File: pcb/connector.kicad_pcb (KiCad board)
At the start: 2 copper layers, 60 x 10 mm, 7 parts

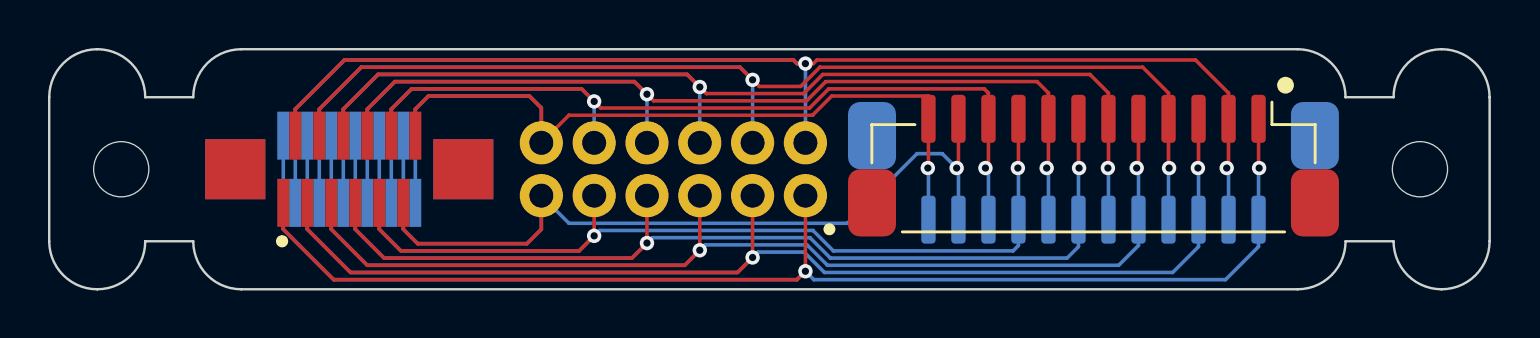
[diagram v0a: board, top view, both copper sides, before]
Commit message: small updates to silkscreen and logo
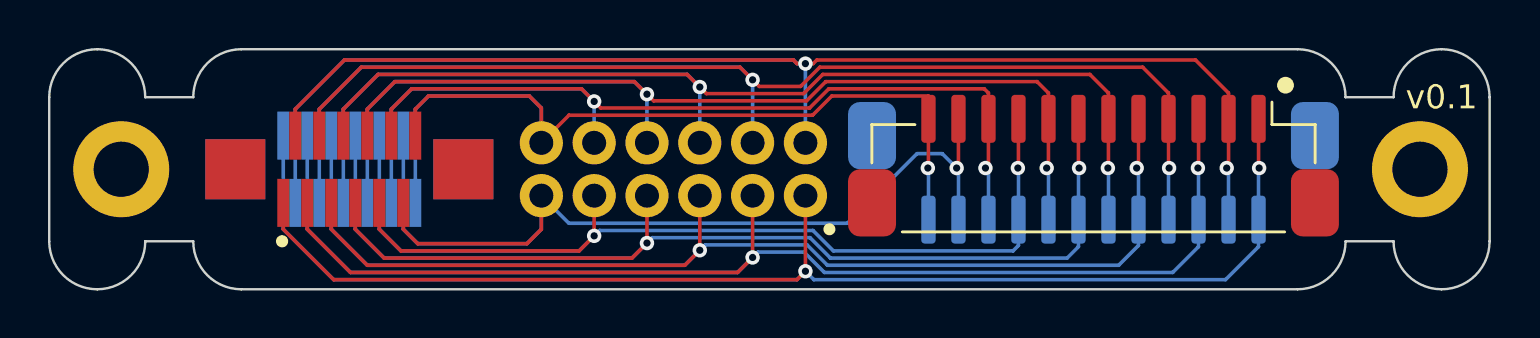
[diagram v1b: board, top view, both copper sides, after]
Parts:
- H1, H2: footprint zzkeeb:Hole_M2 -> zzkeeb:Hole_M2-TH
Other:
- board text added: "v0.1"
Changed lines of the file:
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@@
     )
   )
-  (footprint "zzkeeb:Hole_M2" (layer "F.Cu")
+  (footprint "zzkeeb:Hole_M2-TH" (layer "F.Cu")
     (at 102.583 82.516)
-    (descr "Mounting Hole 2.2mm, no annular, M2")
-    (tags "mounting hole 2.2mm no annular m2")
     (property "Sheetfile" "connector.kicad_sch")
     (property "Sheetname" "")
     (property "ki_description" "Mounting Hole without connection")
     (property "ki_keywords" "mounting hole")
-    (attr exclude_from_pos_files)
-    (fp_text reference "H1" (at -0.95 -0.55) (layer "F.Fab") hide
-        (effects (font (size 1 1) (thickness 0.15)))
-    )
-    (fp_text value "MountingHole" (at 0 0.55) (layer "F.Fab") hide
-        (effects (font (size 1 1) (thickness 0.15)))
-    )
-    (pad "" np_thru_hole circle (at 0 0) (size 2.3 2.3) (drill 2.3) (layers "*.Cu" "*.Mask"))
+    (attr through_hole)
+    (fp_text reference "H1" (at 0 2.8) (layer "F.SilkS") hide
+        (effects (font (size 1 1) (thickness 0.15)))
+    )
+    (fp_text value "MountingHole" (at 0 -2.8) (layer "F.Fab") hide
+        (effects (font (size 1 1) (thickness 0.15)))
+    )
+    (pad "" thru_hole circle (at 0 0) (size 4 4) (drill 2.3) (layers "*.Cu" "*.Mask"))
   )
   (footprint "zzkeeb:Connector_VIK-magnetic-keyboard" (layer "F.Cu")
@@
     )
   )
-  (footprint "zzkeeb:Hole_M2" (layer "F.Cu")
+  (footprint "zzkeeb:Hole_M2-TH" (layer "F.Cu")
     (at 156.683 82.516)
-    (descr "Mounting Hole 2.2mm, no annular, M2")
-    (tags "mounting hole 2.2mm no annular m2")
     (property "Sheetfile" "connector.kicad_sch")
     (property "Sheetname" "")
     (property "ki_description" "Mounting Hole without connection")
     (property "ki_keywords" "mounting hole")
-    (attr exclude_from_pos_files)
-    (fp_text reference "H2" (at -0.95 -0.55) (layer "F.Fab") hide
-        (effects (font (size 1 1) (thickness 0.15)))
-    )
-    (fp_text value "MountingHole" (at 0 0.55) (layer "F.Fab") hide
-        (effects (font (size 1 1) (thickness 0.15)))
-    )
-    (pad "" np_thru_hole circle (at 0 0) (size 2.3 2.3) (drill 2.3) (layers "*.Cu" "*.Mask"))
+    (attr through_hole)
+    (fp_text reference "H2" (at 0 2.8) (layer "F.SilkS") hide
+        (effects (font (size 1 1) (thickness 0.15)))
+    )
+    (fp_text value "MountingHole" (at 0 -2.8) (layer "F.Fab") hide
+        (effects (font (size 1 1) (thickness 0.15)))
+    )
+    (pad "" thru_hole circle (at 0 0) (size 4 4) (drill 2.3) (layers "*.Cu" "*.Mask"))
   )
   (footprint "zzkeeb:Connector_JST-1x12-P1.25mm-vertical" (layer "B.Cu")
@@
   (gr_line (start 153.583 85.516) (end 155.583 85.516)
     (stroke (width 0.1) (type default)) (layer "Edge.Cuts"))
+  (gr_text "v0.1" (at 157.483 79.516) (layer "B.SilkS")
+    (effects (font (size 1 1) (thickness 0.15)) (justify mirror))
+  )
+  (gr_text "v0.1" (at 157.583 79.516) (layer "F.SilkS")
+    (effects (font (size 1 1) (thickness 0.15)))
+  )
   (segment (start 131.083 86.765294) (end 131.083 83.616) (width 0.15) (layer "F.Cu") (net 1))
   (segment (start 130.733 87.116) (end 111.433 87.116) (width 0.15) (layer "F.Cu") (net 1))

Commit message: simplify connector and reduce size
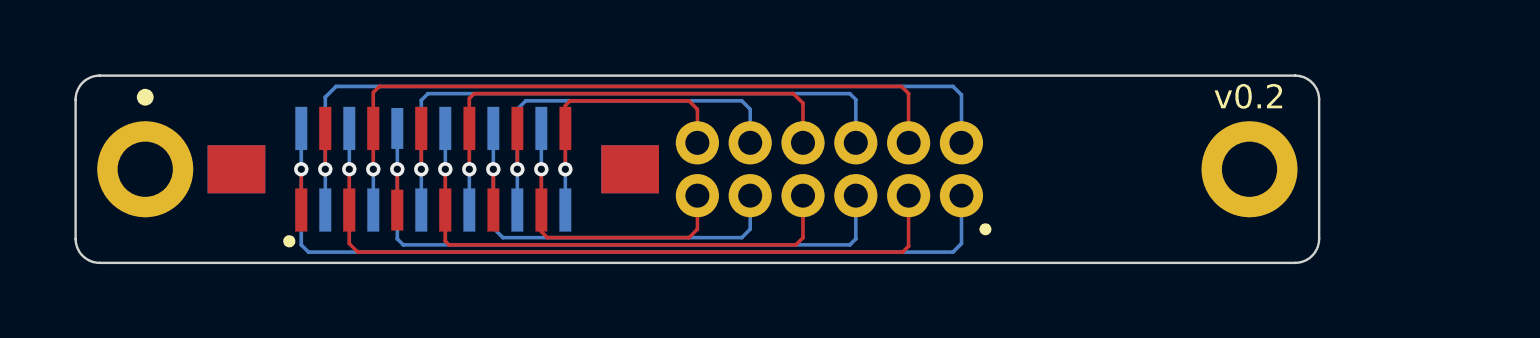
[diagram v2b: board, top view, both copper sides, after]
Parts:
- removed VIK_K3, VIK_K5: Connector_VIK-keyboard, zzkeeb:Connector_JST-1x12-P1.25mm-vertical
- H1: moved to B.Cu
- VIK_K2, VIK_K4: footprint zzkeeb:Connector_VIK-vertical-keyboard -> zzkeeb:Connector_FFC-12pin-1mm-vertical
- moved H2 7.10 mm to (149.6, 82.5)
- moved VIK_K1 6.50 mm to (132.1, 82.5)
- moved VIK_K2 3.50 mm to (115.6, 82.5)
- moved VIK_K4 3.50 mm to (115.6, 82.5)
- moved H1 1.00 mm to (103.6, 82.5), turned to 180 degrees
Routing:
- net Net-(VIK_K1-3V3): track 78.6 -> 36.3 mm, vias 2 -> 1
- net Net-(VIK_K1-SDA): track 71.5 -> 30.4 mm, vias 2 -> 1
- net Net-(VIK_K1-GND-Pad2): track 76.2 -> 35.2 mm, vias 2 -> 1
- net Net-(VIK_K1-SCL): track 69.1 -> 29.5 mm, vias 2 -> 1
- net Net-(VIK_K1-RGB_IN): track 64.1 -> 27.4 mm, vias 2 -> 1
- net Net-(VIK_K1-5V): track 61.7 -> 26.4 mm, vias 2 -> 1
- net Net-(VIK_K1-GND-Pad7): track 56.7 -> 21.5 mm, vias 2 -> 1
- net Net-(VIK_K1-MOSI): track 54.4 -> 20.4 mm, vias 2 -> 1
- net Net-(VIK_K1-MISO): track 43.8 -> 12.4 mm
- net Net-(VIK_K1-GPIO): track 49.3 -> 18.3 mm, vias 2 -> 1
- net Net-(VIK_K1-SCLK): track 41.4 -> 11.5 mm
- net Net-(VIK_K1-CS): track 47.1 -> 17.3 mm, vias 2 -> 1
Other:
- board size 60 x 10 mm -> 51.8 x 7.8 mm
- board text added: "v0.2"
- board text removed: "v0.1"

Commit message: small updates
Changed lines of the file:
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@@
     (fp_circle (center -2.5 6.5) (end -2.7 6.5)
       (stroke (width 0.1) (type solid)) (fill solid) (layer "B.SilkS"))
-    (fp_circle (center -2.5 6.5) (end -2.3 6.5)
+    (fp_circle (center -2.5 6.5) (end -2.25 6.5)
       (stroke (width 0.1) (type solid)) (fill solid) (layer "F.SilkS"))
-    (pad "1" thru_hole circle (at -1.1 5.5 270) (size 1.8 1.8) (drill 1) (layers "*.Cu" "*.Mask")
+    (pad "1" thru_hole circle (at -1.1 5.5 270) (size 1.7 1.7) (drill 0.9) (layers "*.Cu" "*.Mask")
       (net 1 "Net-(VIK_K1-3V3)") (pinfunction "3V3") (pintype "power_in"))
-    (pad "2" thru_hole circle (at 1.1 5.5 270) (size 1.8 1.8) (drill 1) (layers "*.Cu" "*.Mask")
+    (pad "2" thru_hole circle (at 1.1 5.5 270) (size 1.7 1.7) (drill 0.9) (layers "*.Cu" "*.Mask")
       (net 2 "Net-(VIK_K1-GND-Pad2)") (pinfunction "GND") (pintype "power_in"))
-    (pad "3" thru_hole circle (at -1.1 3.3 270) (size 1.8 1.8) (drill 1) (layers "*.Cu" "*.Mask")
+    (pad "3" thru_hole circle (at -1.1 3.3 270) (size 1.7 1.7) (drill 0.9) (layers "*.Cu" "*.Mask")
       (net 3 "Net-(VIK_K1-SDA)") (pinfunction "SDA") (pintype "bidirectional"))
-    (pad "4" thru_hole circle (at 1.1 3.3 270) (size 1.8 1.8) (drill 1) (layers "*.Cu" "*.Mask")
+    (pad "4" thru_hole circle (at 1.1 3.3 270) (size 1.7 1.7) (drill 0.9) (layers "*.Cu" "*.Mask")
       (net 4 "Net-(VIK_K1-SCL)") (pinfunction "SCL") (pintype "bidirectional"))
-    (pad "5" thru_hole circle (at -1.1 1.1 270) (size 1.8 1.8) (drill 1) (layers "*.Cu" "*.Mask")
+    (pad "5" thru_hole circle (at -1.1 1.1 270) (size 1.7 1.7) (drill 0.9) (layers "*.Cu" "*.Mask")
       (net 5 "Net-(VIK_K1-RGB_IN)") (pinfunction "RGB_IN") (pintype "input"))
-    (pad "6" thru_hole circle (at 1.1 1.1 270) (size 1.8 1.8) (drill 1) (layers "*.Cu" "*.Mask")
+    (pad "6" thru_hole circle (at 1.1 1.1 270) (size 1.7 1.7) (drill 0.9) (layers "*.Cu" "*.Mask")
       (net 6 "Net-(VIK_K1-5V)") (pinfunction "5V") (pintype "power_in"))
-    (pad "7" thru_hole circle (at -1.1 -1.1 270) (size 1.8 1.8) (drill 1) (layers "*.Cu" "*.Mask")
+    (pad "7" thru_hole circle (at -1.1 -1.1 270) (size 1.7 1.7) (drill 0.9) (layers "*.Cu" "*.Mask")
       (net 7 "Net-(VIK_K1-GND-Pad7)") (pinfunction "GND") (pintype "power_in"))
-    (pad "8" thru_hole circle (at 1.1 -1.1 270) (size 1.8 1.8) (drill 1) (layers "*.Cu" "*.Mask")
+    (pad "8" thru_hole circle (at 1.1 -1.1 270) (size 1.7 1.7) (drill 0.9) (layers "*.Cu" "*.Mask")
       (net 8 "Net-(VIK_K1-MOSI)") (pinfunction "MOSI") (pintype "input"))
-    (pad "9" thru_hole circle (at -1.1 -3.3 270) (size 1.8 1.8) (drill 1) (layers "*.Cu" "*.Mask")
+    (pad "9" thru_hole circle (at -1.1 -3.3 270) (size 1.7 1.7) (drill 0.9) (layers "*.Cu" "*.Mask")
       (net 9 "Net-(VIK_K1-GPIO)") (pinfunction "GPIO") (pintype "bidirectional"))
-    (pad "10" thru_hole circle (at 1.1 -3.3 270) (size 1.8 1.8) (drill 1) (layers "*.Cu" "*.Mask")
+    (pad "10" thru_hole circle (at 1.1 -3.3 270) (size 1.7 1.7) (drill 0.9) (layers "*.Cu" "*.Mask")
       (net 10 "Net-(VIK_K1-CS)") (pinfunction "CS") (pintype "input"))
-    (pad "11" thru_hole circle (at -1.1 -5.5 270) (size 1.8 1.8) (drill 1) (layers "*.Cu" "*.Mask")
+    (pad "11" thru_hole circle (at -1.1 -5.5 270) (size 1.7 1.7) (drill 0.9) (layers "*.Cu" "*.Mask")
       (net 11 "Net-(VIK_K1-MISO)") (pinfunction "MISO") (pintype "output"))
-    (pad "12" thru_hole circle (at 1.1 -5.5 270) (size 1.8 1.8) (drill 1) (layers "*.Cu" "*.Mask")
+    (pad "12" thru_hole circle (at 1.1 -5.5 270) (size 1.7 1.7) (drill 0.9) (layers "*.Cu" "*.Mask")
       (net 12 "Net-(VIK_K1-SCLK)") (pinfunction "SCLK") (pintype "input"))
     (model "${ZZKEEB}/models/Magnetic connector 12pin male.step"
@@
         (effects (font (size 1 1) (thickness 0.15)))
     )
-    (fp_circle (center -3 -6) (end -2.873 -6)
-      (stroke (width 0.254) (type solid)) (fill none) (layer "F.SilkS"))
+    (fp_circle (center -3 -7) (end -2.75 -7)
+      (stroke (width 0.254) (type solid)) (fill solid) (layer "F.SilkS"))
     (fp_line (start -2.4 -9.6) (end 2.4 -9.6)
       (stroke (width 0.05) (type solid)) (layer "F.CrtYd"))
@@
     (fp_line (start 2.4 9.6) (end -2.4 9.6)
       (stroke (width 0.05) (type solid)) (layer "F.CrtYd"))
-    (pad "" smd rect (at 0 -8.2 90) (size 2 2.4) (layers "F.Cu" "F.Paste" "F.Mask"))
-    (pad "" smd rect (at 0 8.2 90) (size 2 2.4) (layers "F.Cu" "F.Paste" "F.Mask"))
+    (pad "" smd rect (at 0 -8.2 90) (size 2.5 2.5) (layers "F.Cu" "F.Paste" "F.Mask"))
+    (pad "" smd rect (at 0 8.2 90) (size 2.5 2.5) (layers "F.Cu" "F.Paste" "F.Mask"))
     (pad "1" smd rect (at -1.7 -5.5 90) (size 1.8 0.5) (layers "F.Cu" "F.Paste" "F.Mask")
       (net 1 "Net-(VIK_K1-3V3)") (pinfunction "3V3") (pintype "power_in") (thermal_bridge_angle 45))
@@
         (effects (font (size 1 1) (thickness 0.15)) (justify mirror))
     )
-    (fp_circle (center -3 6) (end -2.873 6)
-      (stroke (width 0.254) (type solid)) (fill none) (layer "B.SilkS"))
+    (fp_circle (center -3 7) (end -2.75 7)
+      (stroke (width 0.254) (type solid)) (fill solid) (layer "B.SilkS"))
     (fp_line (start -2.4 -9.6) (end -2.4 9.6)
       (stroke (width 0.05) (type solid)) (layer "B.CrtYd"))
@@
     (fp_line (start 2.4 9.6) (end 2.4 -9.6)
       (stroke (width 0.05) (type solid)) (layer "B.CrtYd"))
-    (pad "" smd rect (at 0 -8.2 270) (size 2 2.4) (layers "B.Cu" "B.Paste" "B.Mask"))
-    (pad "" smd rect (at 0 8.2 270) (size 2 2.4) (layers "B.Cu" "B.Paste" "B.Mask"))
+    (pad "" smd rect (at 0 -8.2 270) (size 2.5 2.5) (layers "B.Cu" "B.Paste" "B.Mask"))
+    (pad "" smd rect (at 0 8.2 270) (size 2.5 2.5) (layers "B.Cu" "B.Paste" "B.Mask"))
     (pad "1" smd rect (at -1.7 5.5 270) (size 1.8 0.5) (layers "B.Cu" "B.Paste" "B.Mask")
       (net 1 "Net-(VIK_K1-3V3)") (pinfunction "3V3") (pintype "power_in") (thermal_bridge_angle 45))
@@
     )
   )
-  (gr_circle (center 103.583 85.516) (end 103.283 85.516)
+  (gr_circle (center 101.783 85.316) (end 102.283 85.316)
     (stroke (width 0.1) (type solid)) (fill solid) (layer "B.SilkS"))
-  (gr_circle (center 103.583 79.516) (end 103.883 79.516)
+  (gr_circle (center 101.783 79.716) (end 102.283 79.716)
     (stroke (width 0.1) (type solid)) (fill solid) (layer "F.SilkS"))
   (gr_line (start 152.483 85.416) (end 152.483 79.616)
@@
   (segment (start 119.083 80.016) (end 119.083 82.516) (width 0.15) (layer "B.Cu") (net 10))
   (segment (start 128.783 80.016) (end 128.433 79.666) (width 0.15) (layer "B.Cu") (net 10))
+  (segment (start 120.233 85.366) (end 126.233 85.366) (width 0.15) (layer "F.Cu") (net 11))
+  (segment (start 126.583 85.016) (end 126.583 83.616) (width 0.15) (layer "F.Cu") (net 11))
+  (segment (start 120.083 85.216) (end 120.233 85.366) (width 0.15) (layer "F.Cu") (net 11))
   (segment (start 126.233 85.366) (end 126.583 85.016) (width 0.15) (layer "F.Cu") (net 11))
-  (segment (start 120.083 84.216) (end 120.083 85.116) (width 0.15) (layer "F.Cu") (net 11))
-  (segment (start 120.083 85.116) (end 120.333 85.366) (width 0.15) (layer "F.Cu") (net 11))
-  (segment (start 126.583 85.016) (end 126.583 83.616) (width 0.15) (layer "F.Cu") (net 11))
-  (segment (start 120.333 85.366) (end 126.233 85.366) (width 0.15) (layer "F.Cu") (net 11))
+  (segment (start 120.083 84.216) (end 120.083 85.216) (width 0.15) (layer "F.Cu") (net 11))
   (segment (start 120.083 82.516) (end 120.083 84.216) (width 0.15) (layer "F.Cu") (net 11))
   (via (at 120.083 82.516) (size 0.6) (drill 0.3) (layers "F.Cu" "B.Cu") (net 11))
